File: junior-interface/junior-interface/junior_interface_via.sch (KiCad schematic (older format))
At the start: 4 parts, among them IC1 6522, IC13 7427, J2 Conn_01x20_Male

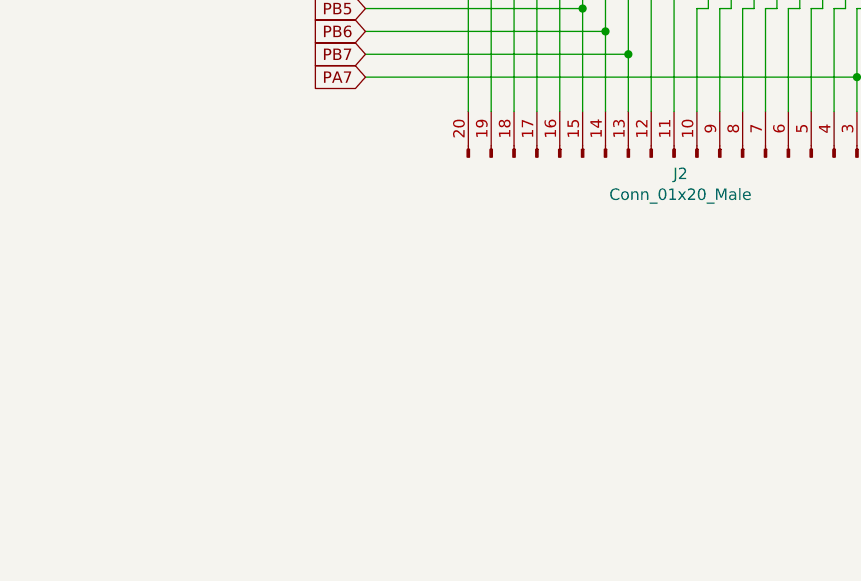
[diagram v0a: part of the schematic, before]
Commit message: junior interface schema
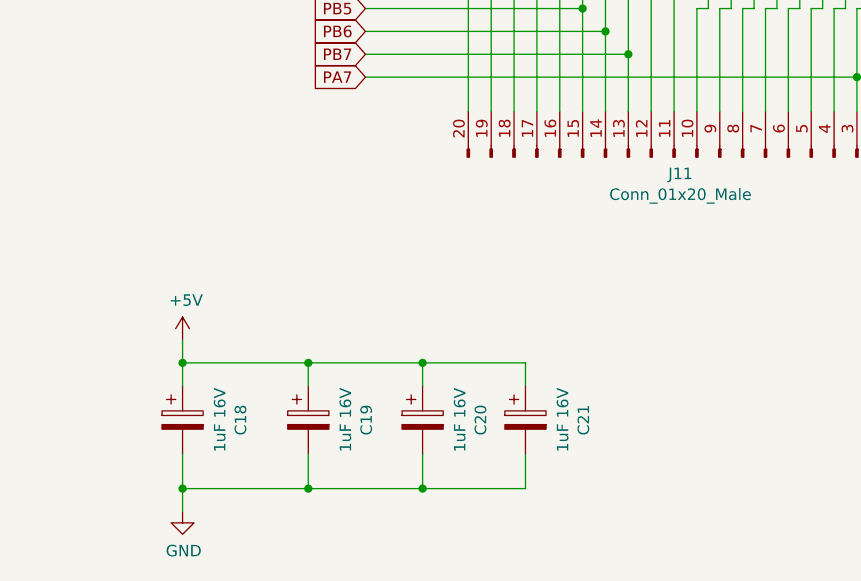
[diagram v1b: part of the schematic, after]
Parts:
- added C18, C19, C20: 1uF 16V, elektor:CAP-POL-3, symbol Device:CP
- added C21: 1uF 16V, elektor:CAP-POL-2, symbol Device:CP
- renumbered J2 to J11
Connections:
- wire segments 87 -> 103
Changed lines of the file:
@@
 $EndDescr
 $Comp
-L Connector:Conn_01x20_Male J2
+L Connector:Conn_01x20_Male J11
 U 1 1 5FDC199D
 P 5350 3850
-F 0 "J2" V 5277 3778 50  0000 C CNN
+F 0 "J11" V 5277 3778 50  0000 C CNN
 F 1 "Conn_01x20_Male" V 5186 3778 50  0000 C CNN
 F 2 "Pin_Headers:Pin_Header_Straight_1x20_Pitch2.54mm" H 5350 3850 50  0001 C CNN
@@
 Wire Wire Line
 	2050 1600 2050 2100
-Wire Bus Line
-	1650 1500 8150 1500
-Wire Bus Line
-	4100 1250 8150 1250
 Text Label 2050 1800 1    50   ~ 0
 AB9
@@
 Text Label 6100 1800 1    50   ~ 0
 DB7
+$Comp
+L power:+5V #PWR0181
+U 1 1 5FCFE822
+P 3100 4650
+F 0 "#PWR0181" H 3100 4500 50  0001 C CNN
+F 1 "+5V" H 3115 4823 50  0000 C CNN
+F 2 "" H 3100 4650 50  0001 C CNN
+F 3 "" H 3100 4650 50  0001 C CNN
+	1    3100 4650
+	1    0    0    -1
+$EndComp
+$Comp
+L power:GND #PWR0182
+U 1 1 5FCFED15
+P 3100 5400
+F 0 "#PWR0182" H 3100 5150 50  0001 C CNN
+F 1 "GND" H 3105 5227 50  0000 C CNN
+F 2 "" H 3100 5400 50  0001 C CNN
+F 3 "" H 3100 5400 50  0001 C CNN
+	1    3100 5400
+	1    0    0    -1
+$EndComp
+$Comp
+L Device:CP C18
+U 1 1 5FCFEF5C
+P 3100 5000
+F 0 "C18" V 3355 5000 50  0000 C CNN
+F 1 "1uF 16V" V 3264 5000 50  0000 C CNN
+F 2 "elektor:CAP-POL-3" H 3138 4850 50  0001 C CNN
+F 3 "~" H 3100 5000 50  0001 C CNN
+	1    3100 5000
+	1    0    0    -1
+$EndComp
+$Comp
+L Device:CP C19
+U 1 1 5FCFF6F6
+P 3650 5000
+F 0 "C19" V 3905 5000 50  0000 C CNN
+F 1 "1uF 16V" V 3814 5000 50  0000 C CNN
+F 2 "elektor:CAP-POL-3" H 3688 4850 50  0001 C CNN
+F 3 "~" H 3650 5000 50  0001 C CNN
+	1    3650 5000
+	1    0    0    -1
+$EndComp
+$Comp
+L Device:CP C20
+U 1 1 5FCFF9F4
+P 4150 5000
+F 0 "C20" V 4405 5000 50  0000 C CNN
+F 1 "1uF 16V" V 4314 5000 50  0000 C CNN
+F 2 "elektor:CAP-POL-3" H 4188 4850 50  0001 C CNN
+F 3 "~" H 4150 5000 50  0001 C CNN
+	1    4150 5000
+	1    0    0    -1
+$EndComp
+$Comp
+L Device:CP C21
+U 1 1 5FCFFF95
+P 4600 5000
+F 0 "C21" V 4855 5000 50  0000 C CNN
+F 1 "1uF 16V" V 4764 5000 50  0000 C CNN
+F 2 "elektor:CAP-POL-2" H 4638 4850 50  0001 C CNN
+F 3 "~" H 4600 5000 50  0001 C CNN
+	1    4600 5000
+	1    0    0    -1
+$EndComp
+Wire Wire Line
+	3100 4650 3100 4750
+Wire Wire Line
+	3100 5150 3100 5300
+Wire Wire Line
+	3100 4750 3650 4750
+Wire Wire Line
+	4600 4750 4600 4850
+Connection ~ 3100 4750
+Wire Wire Line
+	3100 4750 3100 4850
+Wire Wire Line
+	4150 4750 4150 4850
+Connection ~ 4150 4750
+Wire Wire Line
+	4150 4750 4600 4750
+Wire Wire Line
+	3650 4750 3650 4850
+Connection ~ 3650 4750
+Wire Wire Line
+	3650 4750 4150 4750
+Wire Wire Line
+	3100 5300 3650 5300
+Wire Wire Line
+	4600 5300 4600 5150
+Connection ~ 3100 5300
+Wire Wire Line
+	3100 5300 3100 5400
+Wire Wire Line
+	4150 5150 4150 5300
+Connection ~ 4150 5300
+Wire Wire Line
+	4150 5300 4600 5300
+Wire Wire Line
+	3650 5150 3650 5300
+Wire Bus Line
+	1650 1500 8150 1500
+Wire Bus Line
+	4100 1250 8150 1250
+Connection ~ 3650 5300
+Wire Wire Line
+	3650 5300 4150 5300
 $EndSCHEMATC

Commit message: junior interface routage
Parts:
- removed IC13: 7427, symbol 74xx_IEEE:7427
- added IC13: 74LS27, symbol 74xx:74LS27
- added IC14: 74LS01, symbol 74xx:74LS01
- added IC15: 74LS30, symbol 74xx:74LS30
- added IC16: 74LS00, elektor:DIL-14, symbol 74xx:74LS00
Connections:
- wire segments 103 -> 111
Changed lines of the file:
@@
 Wire Wire Line
 	6050 3500 6050 3650
-$Comp
-L 74xx_IEEE:7427 IC13
-U 1 1 6011F85A
-P 2950 2250
-F 0 "IC13" H 2950 1850 50  0000 C CNN
-F 1 "7427" H 2950 1950 50  0000 C CNN
-F 2 "" H 2950 2250 50  0001 C CNN
-F 3 "" H 2950 2250 50  0001 C CNN
-	1    2950 2250
-	1    0    0    -1
-$EndComp
 Wire Wire Line
 	4850 2050 4850 1950
@@
 Wire Wire Line
 	3700 1950 3700 2250
-Wire Wire Line
-	3700 2250 3450 2250
 Text GLabel 2050 2250 0    50   Input ~ 0
 K6
@@
 	2050 2250 2250 2250
 Wire Wire Line
-	2050 2100 2450 2100
-Wire Wire Line
 	2250 2250 2250 1850
 Wire Wire Line
@@
 	4950 1850 4950 2050
 Connection ~ 2250 2250
-Wire Wire Line
-	2250 2250 2450 2250
 $Comp
 L power:GND #PWR0153
 U 1 1 60127BDE
-P 2250 2550
-F 0 "#PWR0153" H 2250 2300 50  0001 C CNN
-F 1 "GND" H 2255 2377 50  0000 C CNN
-F 2 "" H 2250 2550 50  0001 C CNN
-F 3 "" H 2250 2550 50  0001 C CNN
-	1    2250 2550
+P 2400 2500
+F 0 "#PWR0153" H 2400 2250 50  0001 C CNN
+F 1 "GND" H 2405 2327 50  0000 C CNN
+F 2 "" H 2400 2500 50  0001 C CNN
+F 3 "" H 2400 2500 50  0001 C CNN
+	1    2400 2500
 	1    0    0    -1
 $EndComp
@@
 $EndComp
 Wire Wire Line
-	2450 2400 2250 2400
-Wire Wire Line
-	2250 2400 2250 2550
+	2600 2350 2400 2350
+Wire Wire Line
+	2400 2350 2400 2500
 $Comp
 L Device:CP C15
@@
 Entry Wire Line
 	2050 1600 2150 1500
-Wire Wire Line
-	2050 1600 2050 2100
 Text Label 2050 1800 1    50   ~ 0
 AB9
@@
 Wire Wire Line
 	3650 5300 4150 5300
+$Comp
+L 74xx:74LS00 IC16
+U 5 1 5F98447A
+P 6450 5200
+F 0 "IC16" H 6800 5250 50  0000 C CNN
+F 1 "74LS00" H 6800 5150 50  0000 C CNN
+F 2 "elektor:DIL-14" H 6450 5200 50  0001 C CNN
+F 3 "http://www.ti.com/lit/gpn/sn74ls00" H 6450 5200 50  0001 C CNN
+	5    6450 5200
+	1    0    0    -1
+$EndComp
+$Comp
+L power:+5V #PWR0112
+U 1 1 5F984480
+P 6450 4600
+F 0 "#PWR0112" H 6450 4450 50  0001 C CNN
+F 1 "+5V" H 6465 4773 50  0000 C CNN
+F 2 "" H 6450 4600 50  0001 C CNN
+F 3 "" H 6450 4600 50  0001 C CNN
+	1    6450 4600
+	1    0    0    -1
+$EndComp
+$Comp
+L power:GND #PWR0130
+U 1 1 5F984486
+P 6450 5800
+F 0 "#PWR0130" H 6450 5550 50  0001 C CNN
+F 1 "GND" H 6455 5627 50  0000 C CNN
+F 2 "" H 6450 5800 50  0001 C CNN
+F 3 "" H 6450 5800 50  0001 C CNN
+	1    6450 5800
+	1    0    0    -1
+$EndComp
+Wire Wire Line
+	6450 4600 6450 4700
+Wire Wire Line
+	6450 5700 6450 5800
+$Comp
+L 74xx:74LS01 IC14
+U 5 1 5F995632
+P 7300 5200
+F 0 "IC14" H 7530 5246 50  0000 L CNN
+F 1 "74LS01" H 7530 5155 50  0000 L CNN
+F 2 "" H 7300 5200 50  0001 C CNN
+F 3 "http://www.nteinc.com/specs/7400to7499/pdf/nte74LS01.pdf" H 7300 5200 50  0001 C CNN
+	5    7300 5200
+	1    0    0    -1
+$EndComp
+$Comp
+L power:+5V #PWR0131
+U 1 1 5F99821A
+P 7300 4600
+F 0 "#PWR0131" H 7300 4450 50  0001 C CNN
+F 1 "+5V" H 7315 4773 50  0000 C CNN
+F 2 "" H 7300 4600 50  0001 C CNN
+F 3 "" H 7300 4600 50  0001 C CNN
+	1    7300 4600
+	1    0    0    -1
+$EndComp
+$Comp
+L power:GND #PWR0185
+U 1 1 5F9985DD
+P 7300 5800
+F 0 "#PWR0185" H 7300 5550 50  0001 C CNN
+F 1 "GND" H 7305 5627 50  0000 C CNN
+F 2 "" H 7300 5800 50  0001 C CNN
+F 3 "" H 7300 5800 50  0001 C CNN
+	1    7300 5800
+	1    0    0    -1
+$EndComp
+Wire Wire Line
+	7300 4600 7300 4700
+Wire Wire Line
+	7300 5700 7300 5800
+$Comp
+L power:+5V #PWR0186
+U 1 1 5F9A267A
+P 8150 4600
+F 0 "#PWR0186" H 8150 4450 50  0001 C CNN
+F 1 "+5V" H 8165 4773 50  0000 C CNN
+F 2 "" H 8150 4600 50  0001 C CNN
+F 3 "" H 8150 4600 50  0001 C CNN
+	1    8150 4600
+	1    0    0    -1
+$EndComp
+$Comp
+L power:GND #PWR0187
+U 1 1 5F9A2A8F
+P 8150 5800
+F 0 "#PWR0187" H 8150 5550 50  0001 C CNN
+F 1 "GND" H 8155 5627 50  0000 C CNN
+F 2 "" H 8150 5800 50  0001 C CNN
+F 3 "" H 8150 5800 50  0001 C CNN
+	1    8150 5800
+	1    0    0    -1
+$EndComp
+Wire Wire Line
+	8150 4600 8150 4700
+Wire Wire Line
+	8150 5700 8150 5800
+$Comp
+L 74xx:74LS27 IC13
+U 4 1 5F9AADB5
+P 8150 5200
+F 0 "IC13" H 8380 5246 50  0000 L CNN
+F 1 "74LS27" H 8380 5155 50  0000 L CNN
+F 2 "" H 8150 5200 50  0001 C CNN
+F 3 "http://www.ti.com/lit/gpn/sn74LS27" H 8150 5200 50  0001 C CNN
+	4    8150 5200
+	1    0    0    -1
+$EndComp
+$Comp
+L 74xx:74LS30 IC15
+U 2 1 5F9AD05B
+P 9000 5200
+F 0 "IC15" H 9230 5246 50  0000 L CNN
+F 1 "74LS30" H 9230 5155 50  0000 L CNN
+F 2 "" H 9000 5200 50  0001 C CNN
+F 3 "http://www.ti.com/lit/gpn/sn74LS30" H 9000 5200 50  0001 C CNN
+	2    9000 5200
+	1    0    0    -1
+$EndComp
+$Comp
+L power:+5V #PWR0188
+U 1 1 5F9AE23D
+P 9000 4600
+F 0 "#PWR0188" H 9000 4450 50  0001 C CNN
+F 1 "+5V" H 9015 4773 50  0000 C CNN
+F 2 "" H 9000 4600 50  0001 C CNN
+F 3 "" H 9000 4600 50  0001 C CNN
+	1    9000 4600
+	1    0    0    -1
+$EndComp
+$Comp
+L power:GND #PWR0189
+U 1 1 5F9AE586
+P 9000 5800
+F 0 "#PWR0189" H 9000 5550 50  0001 C CNN
+F 1 "GND" H 9005 5627 50  0000 C CNN
+F 2 "" H 9000 5800 50  0001 C CNN
+F 3 "" H 9000 5800 50  0001 C CNN
+	1    9000 5800
+	1    0    0    -1
+$EndComp
+Wire Wire Line
+	9000 4600 9000 4700
+Wire Wire Line
+	9000 5700 9000 5800
+$Comp
+L 74xx:74LS27 IC13
+U 1 1 5FA52255
+P 2900 2250
+F 0 "IC13" H 2900 2575 50  0000 C CNN
+F 1 "74LS27" H 2900 2484 50  0000 C CNN
+F 2 "" H 2900 2250 50  0001 C CNN
+F 3 "http://www.ti.com/lit/gpn/sn74LS27" H 2900 2250 50  0001 C CNN
+	1    2900 2250
+	1    0    0    -1
+$EndComp
+Wire Wire Line
+	3200 2250 3700 2250
+Wire Wire Line
+	2250 2250 2600 2250
+Wire Wire Line
+	2600 2150 2050 2150
 Wire Bus Line
 	1650 1500 8150 1500
 Wire Bus Line
 	4100 1250 8150 1250
+Wire Wire Line
+	2050 1600 2050 2150
 $EndSCHEMATC

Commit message: junior interface routage
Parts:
- added J13: +12V, elektor:PIN, symbol Connector:Conn_01x01_Male
- added J14: -5V, elektor:PIN, symbol Connector:Conn_01x01_Male
- added J15: -12V, elektor:PIN, symbol Connector:Conn_01x01_Male
- added J16: 0, elektor:PIN, symbol Connector:Conn_01x01_Male
- added J17, J18, J19, J20, J21, J22, J23, J3, J5: (no value), elektor:PIN, symbol Connector:Conn_01x01_Male
- added J8: +5V, elektor:PIN, symbol Connector:Conn_01x01_Male
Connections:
- net +5V: now also J17.1 (Pin_1), J18.1 (Pin_1), J19.1 (Pin_1), J20.1 (Pin_1), J8.1 (Pin_1)
- net GND: now also J16.1 (Pin_1)
- net PA7: now also J11.8 (Pin_8), J23.1 (Pin_1); no longer J11.3 (Pin_3)
- net PB0: now also J11.9 (Pin_9), J3.1 (Pin_1); no longer J11.20 (Pin_20)
- net PB5: now also J11.14 (Pin_14), J5.1 (Pin_1); no longer J11.15 (Pin_15)
- net PB6: now also J11.15 (Pin_15), J21.1 (Pin_1); no longer J11.14 (Pin_14)
- net PB7: now also J11.16 (Pin_16), J22.1 (Pin_1); no longer J11.13 (Pin_13)
- net at J11.1 (Pin_1): now also IC1.2 (PA0); no longer IC1.40 (CA1)
- net at J11.10 (Pin_10): now also IC1.11 (PB1); no longer IC1.2 (PA0)
- net at J11.11 (Pin_11): now also IC1.12 (PB2); no longer IC1.18 (CB1)
- net at J11.12 (Pin_12): now also IC1.13 (PB3); no longer IC1.19 (CB2)
- net at IC1.14 (PB4): now also J11.13 (Pin_13); no longer J11.16 (Pin_16)
- net at J11.17 (Pin_17): now also IC1.18 (CB1); no longer IC1.13 (PB3)
- net at J11.18 (Pin_18): now also IC1.19 (CB2); no longer IC1.12 (PB2)
- net at J11.19 (Pin_19): now also IC1.39 (CA2); no longer IC1.11 (PB1)
- net at J11.2 (Pin_2): now also IC1.3 (PA1); no longer IC1.39 (CA2)
- net at J11.4 (Pin_4): now also IC1.5 (PA3); no longer IC1.8 (PA6)
- net at J11.5 (Pin_5): now also IC1.6 (PA4); no longer IC1.7 (PA5)
- net at J11.6 (Pin_6): now also IC1.7 (PA5); no longer IC1.6 (PA4)
- net at J11.7 (Pin_7): now also IC1.8 (PA6); no longer IC1.5 (PA3)
- net at IC1.4 (PA2): now also J11.3 (Pin_3); no longer J11.8 (Pin_8)
- new net: IC1.40 (CA1), J11.20 (Pin_20)
- new net +12V: J13.1 (Pin_1)
- new net -12V: J15.1 (Pin_1)
- new net -5V: J14.1 (Pin_1)
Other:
- moved on the sheet: C18, C19, C20, C21, IC13D, IC14E, IC15B, IC16E, J11

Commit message: junior interface routage
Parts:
- added C16: 1uF 16V, elektor:CAP-POL-3, symbol Device:CP
- added C17: 1uF 16V, elektor:CAP-POL-2.5, symbol Device:CP
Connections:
- net +12V: now also C17.1
- net -5V: now also C16.2
- net GND: now also C16.1, C17.2
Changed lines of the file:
@@
 Wire Wire Line
 	3950 3700 3950 3400
+Connection ~ 3950 3400
+Wire Wire Line
+	3950 3400 5050 3400
+$Comp
+L power:GND #PWR0198
+U 1 1 5F9C5531
+P 4600 6900
+F 0 "#PWR0198" H 4600 6650 50  0001 C CNN
+F 1 "GND" H 4605 6727 50  0000 C CNN
+F 2 "" H 4600 6900 50  0001 C CNN
+F 3 "" H 4600 6900 50  0001 C CNN
+	1    4600 6900
+	1    0    0    -1
+$EndComp
+$Comp
+L Device:CP C16
+U 1 1 5F9C5537
+P 4600 6500
+F 0 "C16" V 4855 6500 50  0000 C CNN
+F 1 "1uF 16V" V 4764 6500 50  0000 C CNN
+F 2 "elektor:CAP-POL-3" H 4638 6350 50  0001 C CNN
+F 3 "~" H 4600 6500 50  0001 C CNN
+	1    4600 6500
+	-1   0    0    1
+$EndComp
+$Comp
+L power:GND #PWR0199
+U 1 1 5F9CD81C
+P 5550 6900
+F 0 "#PWR0199" H 5550 6650 50  0001 C CNN
+F 1 "GND" H 5555 6727 50  0000 C CNN
+F 2 "" H 5550 6900 50  0001 C CNN
+F 3 "" H 5550 6900 50  0001 C CNN
+	1    5550 6900
+	1    0    0    -1
+$EndComp
+$Comp
+L Device:CP C17
+U 1 1 5F9CD822
+P 5550 6500
+F 0 "C17" V 5805 6500 50  0000 C CNN
+F 1 "1uF 16V" V 5714 6500 50  0000 C CNN
+F 2 "elektor:CAP-POL-2.5" H 5588 6350 50  0001 C CNN
+F 3 "~" H 5550 6500 50  0001 C CNN
+	1    5550 6500
+	1    0    0    -1
+$EndComp
+Wire Wire Line
+	5550 6150 5550 6350
+Wire Wire Line
+	5550 6650 5550 6900
+Wire Wire Line
+	4600 6150 4600 6350
+Wire Wire Line
+	4600 6650 4600 6900
+$Comp
+L power:-5V #PWR0200
+U 1 1 5F9F73FB
+P 4600 6150
+F 0 "#PWR0200" H 4600 6250 50  0001 C CNN
+F 1 "-5V" V 4615 6278 50  0000 L CNN
+F 2 "" H 4600 6150 50  0001 C CNN
+F 3 "" H 4600 6150 50  0001 C CNN
+	1    4600 6150
+	1    0    0    -1
+$EndComp
+$Comp
+L power:+12V #PWR0201
+U 1 1 5F9F79B1
+P 5550 6150
+F 0 "#PWR0201" H 5550 6000 50  0001 C CNN
+F 1 "+12V" V 5565 6278 50  0000 L CNN
+F 2 "" H 5550 6150 50  0001 C CNN
+F 3 "" H 5550 6150 50  0001 C CNN
+	1    5550 6150
+	1    0    0    -1
+$EndComp
 Wire Bus Line
 	1650 1500 8150 1500
 Wire Bus Line
 	4100 1250 8150 1250
-Connection ~ 3950 3400
-Wire Wire Line
-	3950 3400 5050 3400
 $EndSCHEMATC
